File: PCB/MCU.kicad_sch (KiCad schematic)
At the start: 0 parts

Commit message: feat(Sheets): Added IC and Power sheets
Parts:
- added PS1: HLK-PM03, Converter_ACDC:Converter_ACDC_Hi-Link_HLK-PMxx, symbol Converter_ACDC:HLK-PM03
- added U1: ESP-12F, RF_Module:ESP-12E, symbol RF_Module:ESP-12F
- added U2: ATM90E26-YU, Package_SO:SSOP-28_5.3x10.2mm_P0.65mm, symbol Sensor_Energy:ATM90E26-YU
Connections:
- new net: U2.14 (AGND), U2.6 (AGND)
- new net: U2.2 (DGND), U2.9 (DGND)

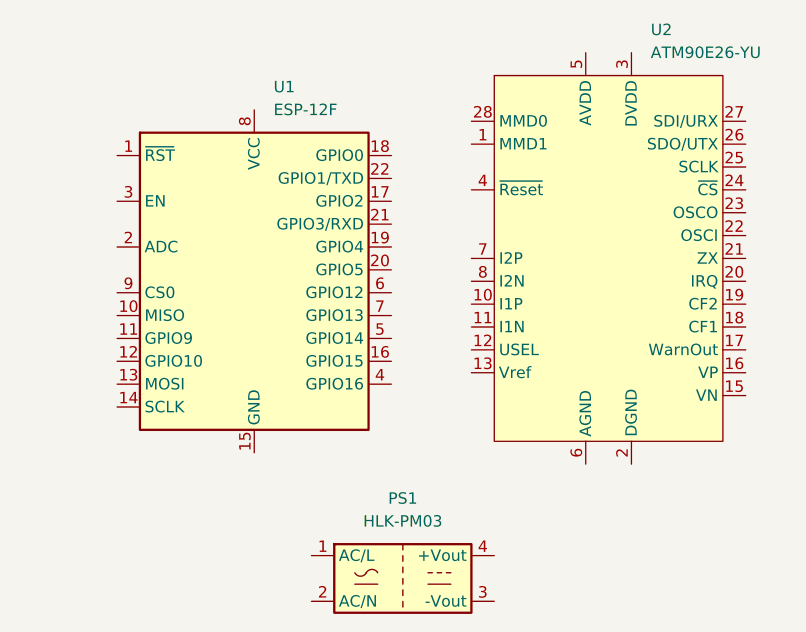
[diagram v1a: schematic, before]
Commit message: feat(POWER): introduced a dual ldo power tree with a 230-5v supply
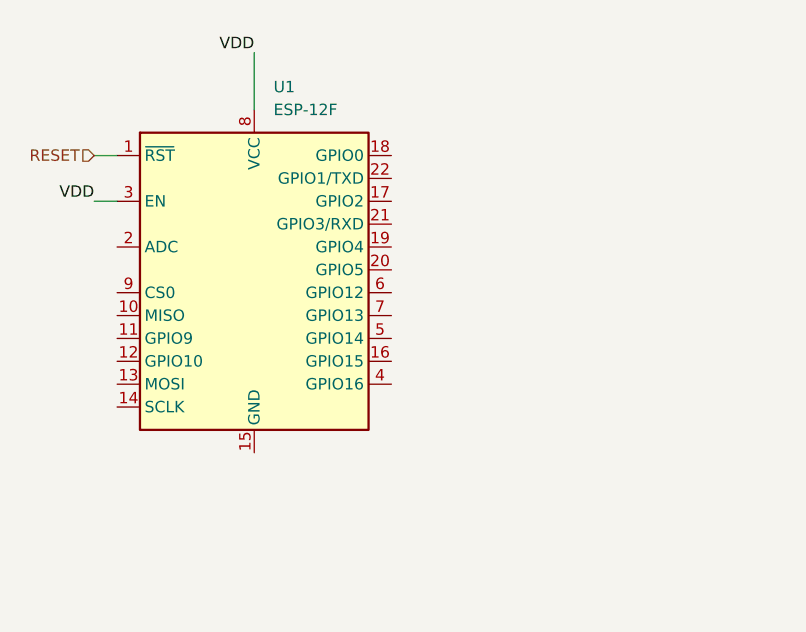
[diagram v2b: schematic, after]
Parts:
- removed PS1: HLK-PM03, Converter_ACDC:Converter_ACDC_Hi-Link_HLK-PMxx, symbol Converter_ACDC:HLK-PM03
- removed U2: ATM90E26-YU, Package_SO:SSOP-28_5.3x10.2mm_P0.65mm, symbol Sensor_Energy:ATM90E26-YU
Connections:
- net RESET: now reaches U1.1 (~{RST})
- net VDD: now reaches U1.3 (EN)
- net VDD: now also U1.8 (VCC)
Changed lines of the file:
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@@
 	(generator_version "9.0")
 	(paper "A4")
+	(wire
+		(pts
+			(xy 125.73 74.93) (xy 128.27 74.93)
+		)
+		(stroke
+			(width 0)
+			(type default)
+		)
+	)
+	(wire
+		(pts
+			(xy 143.51 63.5) (xy 143.51 69.85)
+		)
+		(stroke
+			(width 0)
+			(type default)
+		)
+	)
+	(wire
+		(pts
+			(xy 125.73 80.01) (xy 128.27 80.01)
+		)
+		(stroke
+			(width 0)
+			(type default)
+		)
+	)
+	(label "VDD"
+		(at 143.51 63.5 180)
+		(effects
+			(font
+				(size 1.27 1.27)
+			)
+			(justify right bottom)
+		)
+	)
+	(label "VDD"
+		(at 125.73 80.01 180)
+		(effects
+			(font
+				(size 1.27 1.27)
+			)
+			(justify right bottom)
+		)
+	)
+	(hierarchical_label "RESET"
+		(shape input)
+		(at 125.73 74.93 180)
+		(effects
+			(font
+				(size 1.27 1.27)
+			)
+			(justify right)
+		)
+	)
 	(symbol
 		(lib_id "RF_Module:ESP-12F")
@@
 					(unit 1)
 				)
-			)
-		)
-	)
-	(symbol
-		(lib_id "Converter_ACDC:HLK-PM03")
-		(at 160.02 121.92 0)
-		(unit 1)
-		(exclude_from_sim no)
-		(in_bom yes)
-		(on_board yes)
-		(dnp no)
-		(fields_autoplaced yes)
-		(property "Reference" "PS1"
-			(at 160.02 113.03 0)
-			(effects
-				(font
-					(size 1.27 1.27)
-				)
-			)
-		)
-		(property "Value" "HLK-PM03"
-			(at 160.02 115.57 0)
-			(effects
-				(font
-					(size 1.27 1.27)
-				)
-			)
-		)
-		(property "Footprint" "Converter_ACDC:Converter_ACDC_Hi-Link_HLK-PMxx"
-			(at 160.02 129.54 0)
-			(effects
-				(font
-					(size 1.27 1.27)
-				)
-				(hide yes)
-			)
-		)
-		(property "Datasheet" "https://h.hlktech.com/download/ACDC%E7%94%B5%E6%BA%90%E6%A8%A1%E5%9D%973W%E7%B3%BB%E5%88%97/1/%E6%B5%B7%E5%87%8C%E7%A7%913W%E7%B3%BB%E5%88%97%E7%94%B5%E6%BA%90%E6%A8%A1%E5%9D%97%E8%A7%84%E6%A0%BC%E4%B9%A6V2.8.pdf"
-			(at 170.18 130.81 0)
-			(effects
-				(font
-					(size 1.27 1.27)
-				)
-				(hide yes)
-			)
-		)
-		(property "Description" "Compact AC/DC board mount power module 3W 3V3"
-			(at 160.02 121.92 0)
-			(effects
-				(font
-					(size 1.27 1.27)
-				)
-				(hide yes)
-			)
-		)
-		(pin "2"
-		)
-		(pin "1"
-		)
-		(pin "3"
-		)
-		(pin "4"
-		)
-		(instances
-			(project ""
-				(path "/b3a00096-e201-45d6-8313-ccf00a75c96f/f6d29f19-82be-493b-ac03-8f5d2874d778"
-					(reference "PS1")
-					(unit 1)
-				)
-			)
-		)
-	)
-	(symbol
-		(lib_id "Sensor_Energy:ATM90E26-YU")
-		(at 182.88 86.36 0)
-		(unit 1)
-		(exclude_from_sim no)
-		(in_bom yes)
-		(on_board yes)
-		(dnp no)
-		(fields_autoplaced yes)
-		(property "Reference" "U2"
-			(at 187.5633 60.96 0)
-			(effects
-				(font
-					(size 1.27 1.27)
-				)
-				(justify left)
-			)
-		)
-		(property "Value" "ATM90E26-YU"
-			(at 187.5633 63.5 0)
-			(effects
-				(font
-					(size 1.27 1.27)
-				)
-				(justify left)
-			)
-		)
-		(property "Footprint" "Package_SO:SSOP-28_5.3x10.2mm_P0.65mm"
-			(at 210.82 109.22 0)
-			(effects
-				(font
-					(size 1.27 1.27)
-				)
-				(hide yes)
-			)
-		)
-		(property "Datasheet" "https://ww1.microchip.com/downloads/aemDocuments/documents/OTH/ProductDocuments/DataSheets/Atmel-46002-SE-M90E26-Datasheet.pdf"
-			(at 182.88 86.36 0)
-			(effects
-				(font
-					(size 1.27 1.27)
-				)
-				(hide yes)
-			)
-		)
-		(property "Description" "High precision energy metering device for single-phase two-wire and single-phase three-wire, SSOP-28"
-			(at 182.88 86.36 0)
-			(effects
-				(font
-					(size 1.27 1.27)
-				)
-				(hide yes)
-			)
-		)
-		(pin "21"
-		)
-		(pin "24"
-		)
-		(pin "20"
-		)
-		(pin "12"
-		)
-		(pin "23"
-		)
-		(pin "22"
-		)
-		(pin "6"
-		)
-		(pin "13"
-		)
-		(pin "3"
-		)
-		(pin "7"
-		)
-		(pin "11"
-		)
-		(pin "10"
-		)
-		(pin "8"
-		)
-		(pin "4"
-		)
-		(pin "1"
-		)
-		(pin "28"
-		)
-		(pin "17"
-		)
-		(pin "14"
-		)
-		(pin "27"
-		)
-		(pin "5"
-		)
-		(pin "16"
-		)
-		(pin "15"
-		)
-		(pin "26"
-		)
-		(pin "9"
-		)
-		(pin "2"
-		)
-		(pin "19"
-		)
-		(pin "25"
-		)
-		(pin "18"
-		)
-		(instances
-			(project ""
-				(path "/b3a00096-e201-45d6-8313-ccf00a75c96f/f6d29f19-82be-493b-ac03-8f5d2874d778"
-					(reference "U2")
-					(unit 1)
-				)

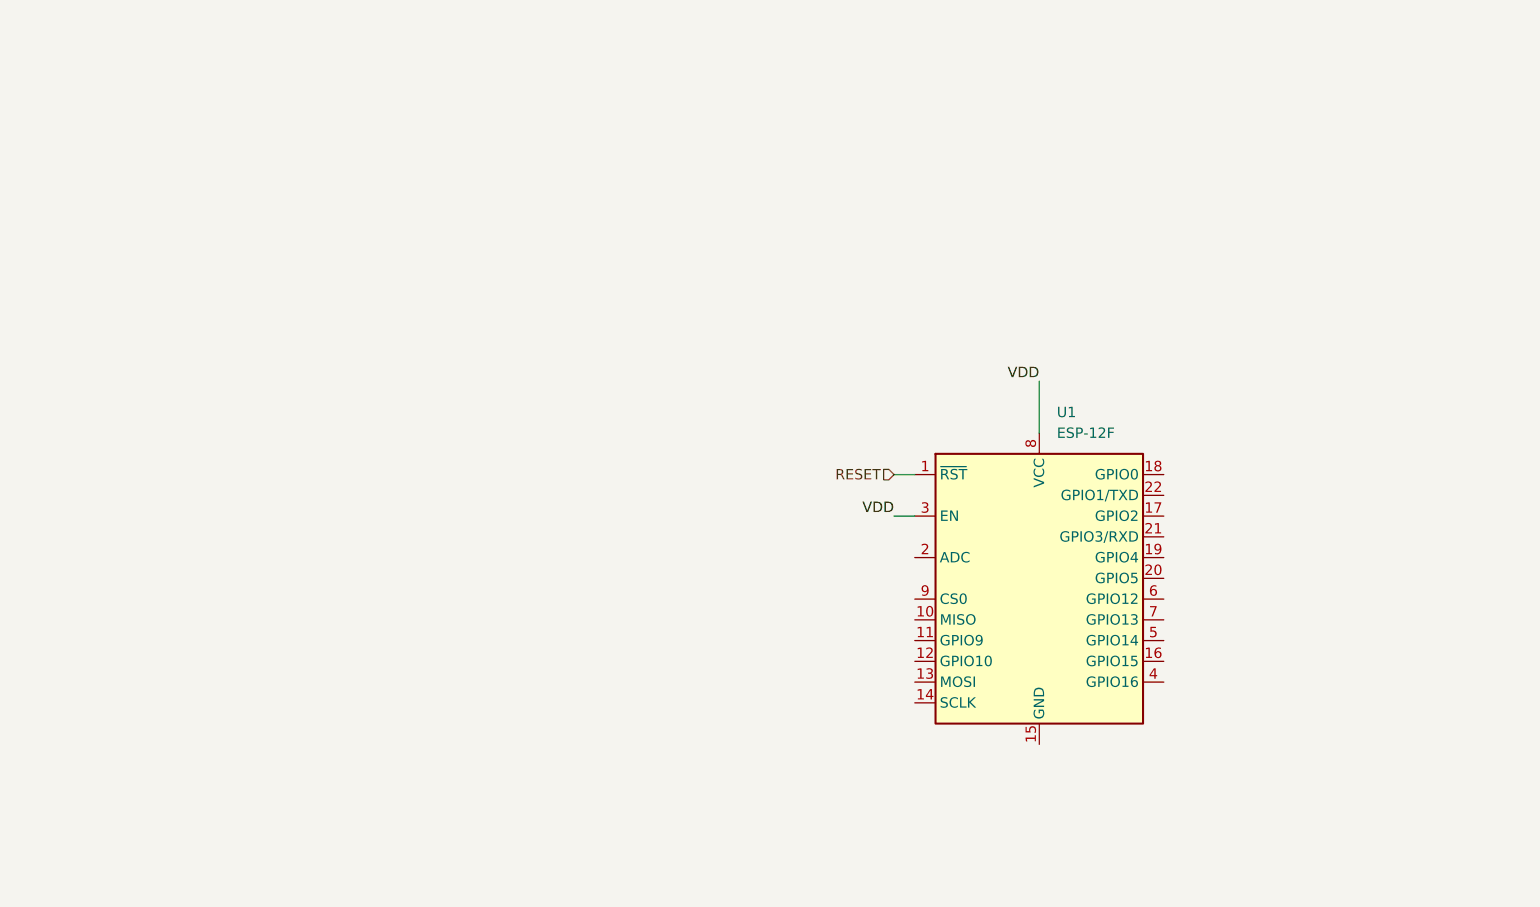
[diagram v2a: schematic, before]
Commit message: added firmware dir
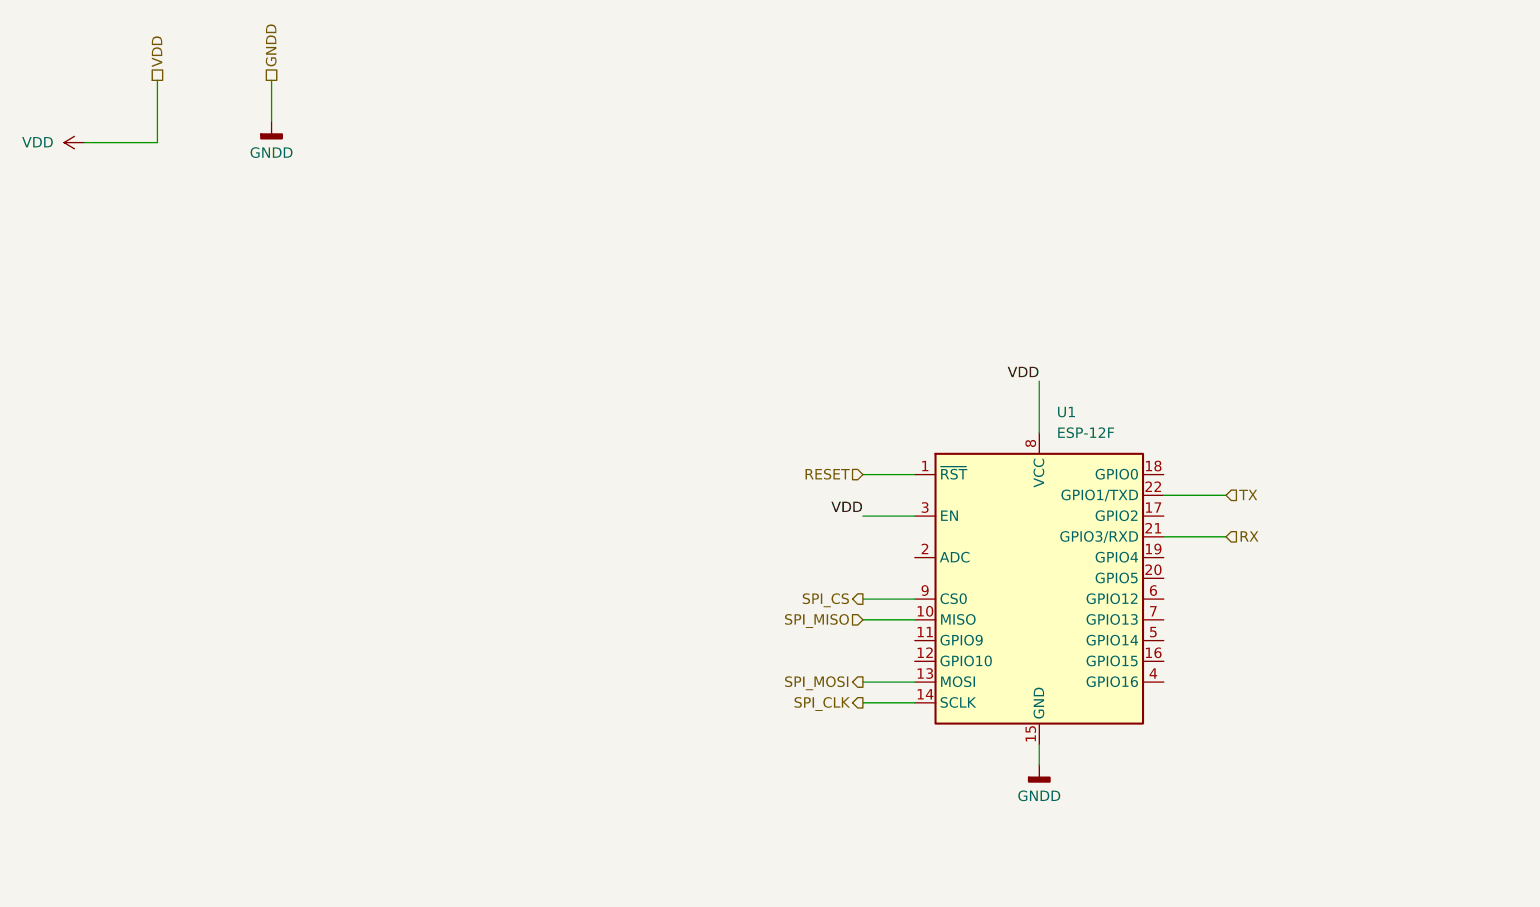
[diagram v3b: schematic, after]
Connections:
- net SPI_MISO: now reaches U1.10 (MISO)
- net SPI_MOSI: now reaches U1.13 (MOSI)
- net SPI_CLK: now reaches U1.14 (SCLK)
- net GNDD: now reaches U1.15 (GND)
- net RX: now reaches U1.21 (GPIO3/RXD)
- net TX: now reaches U1.22 (GPIO1/TXD)
- net SPI_CS: now reaches U1.9 (CS0)
